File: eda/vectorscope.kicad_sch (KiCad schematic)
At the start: 76 parts, among them J1 EXT PWR, J2 IO CONNECTOR, J3 SCOPE, J4 SIGGEN, P1 IO_PLUG_USB, Q1 DMG2301L, SW1 USER, SW10 MENU, SW11 LEVEL, SW12 RANGE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

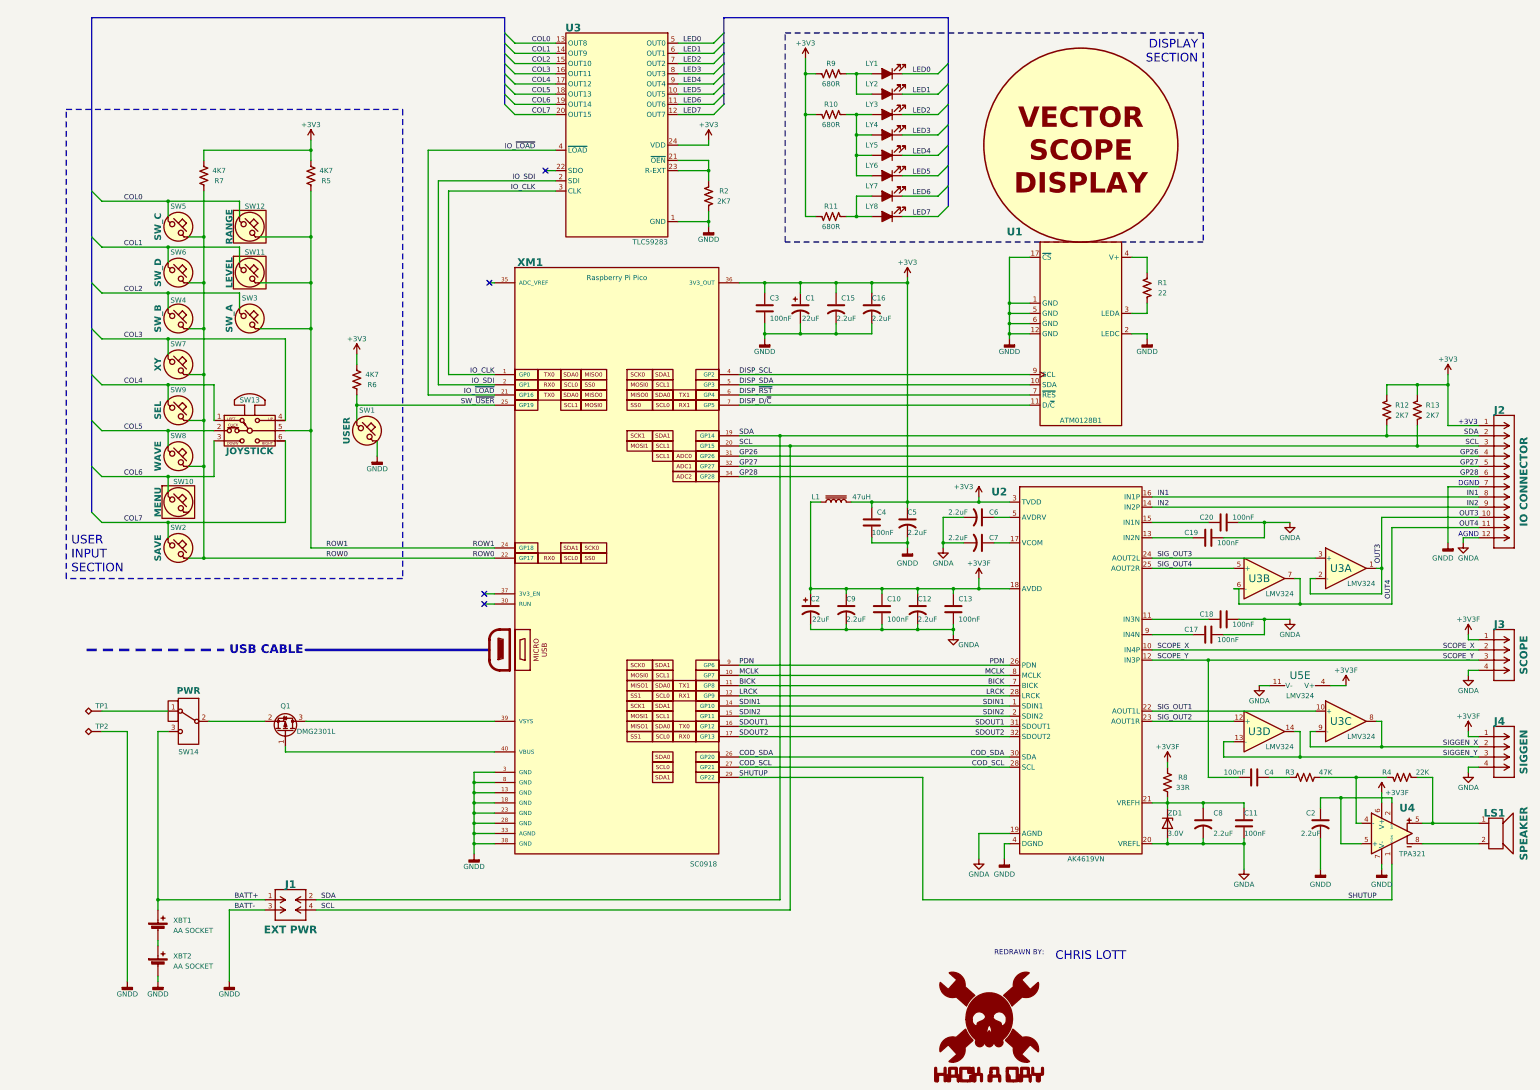
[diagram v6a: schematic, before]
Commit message: cleaned up schematic some, solved some DRC errors
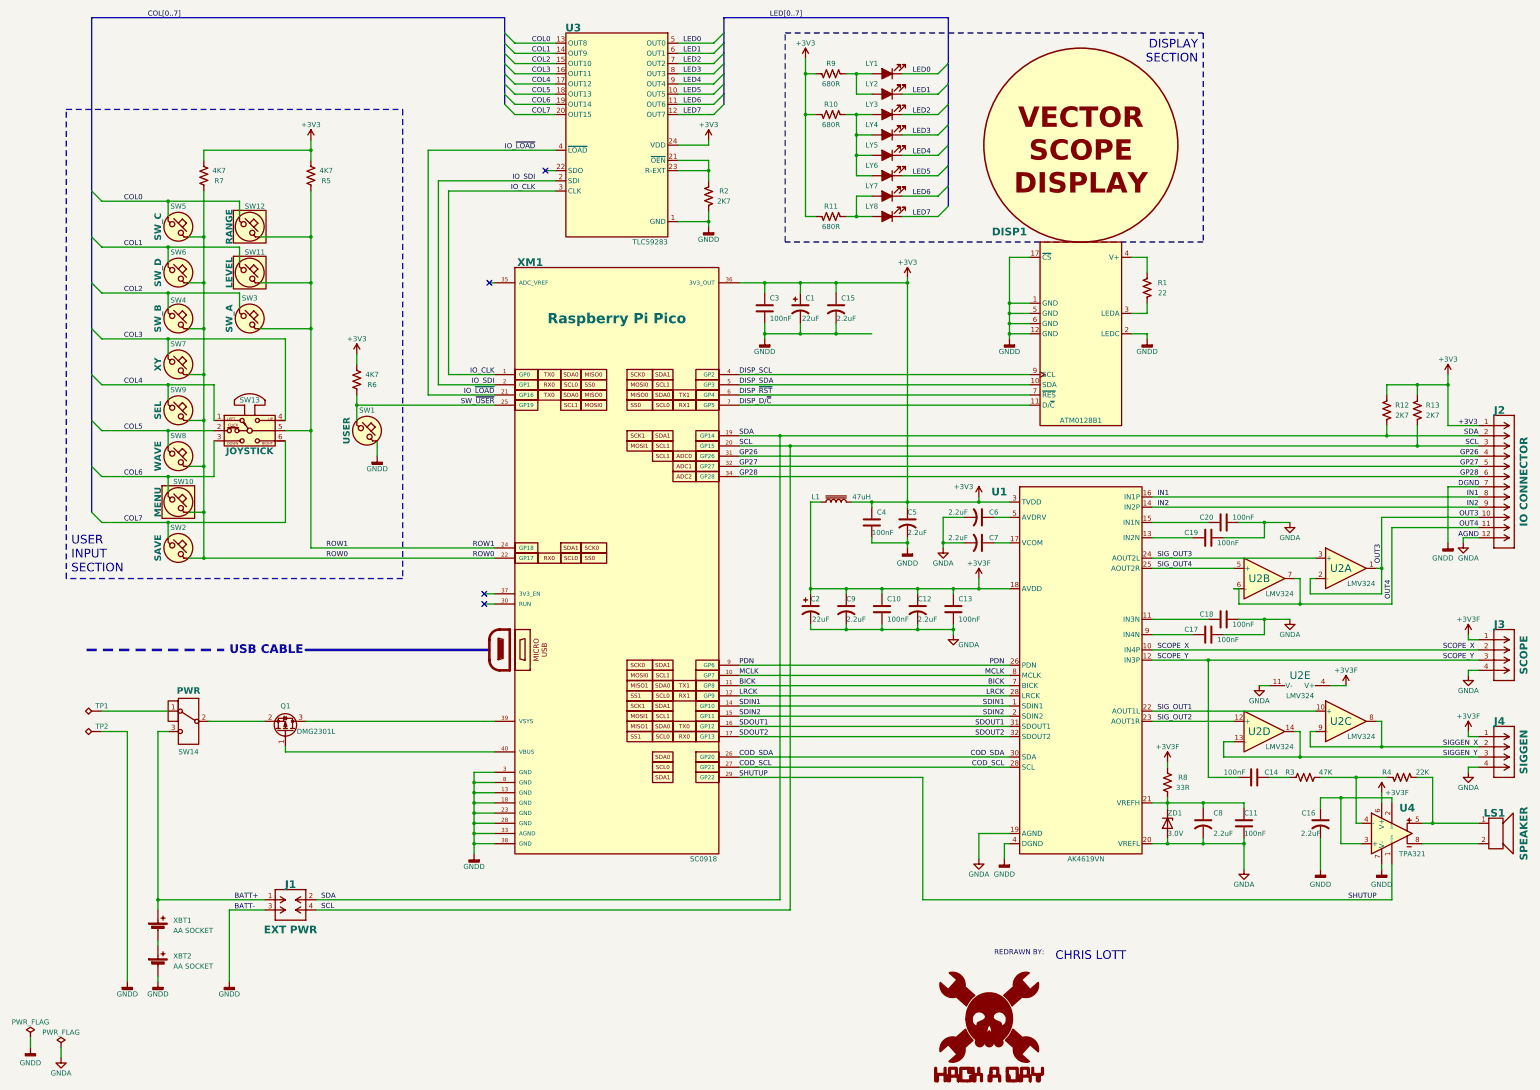
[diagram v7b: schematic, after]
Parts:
- removed C16: 2.2uF, symbol .stumbler:CAP
- P1: now left out of the parts list
- U2: renamed from U3; symbol Amplifier_Operational:LMV324 -> .vector:LMV324
- U2: renamed from U5; symbol Amplifier_Operational:LMV324 -> .vector:LMV324
- renumbered C4 to C14, C2 to C16, U1 to DISP1, U2 to U1
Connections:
- net ROW0: now also SW10.2
- net at C16.1, U4.2 (BYP): now also U4.3 (+); no longer U4.5
- net +3V3F: no longer names the net of C10.1, C12.1, C13.1, C2.1, C9.1, L1.2, U1.18 (AVDD)
- net +3V3F: no longer J3.1 (Pin_1), J4.1 (Pin_1), R8.2, U2.4 (V+), U4.6 (V+)
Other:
- note added: "BATT-"

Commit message: all schematic symbols now in local project library
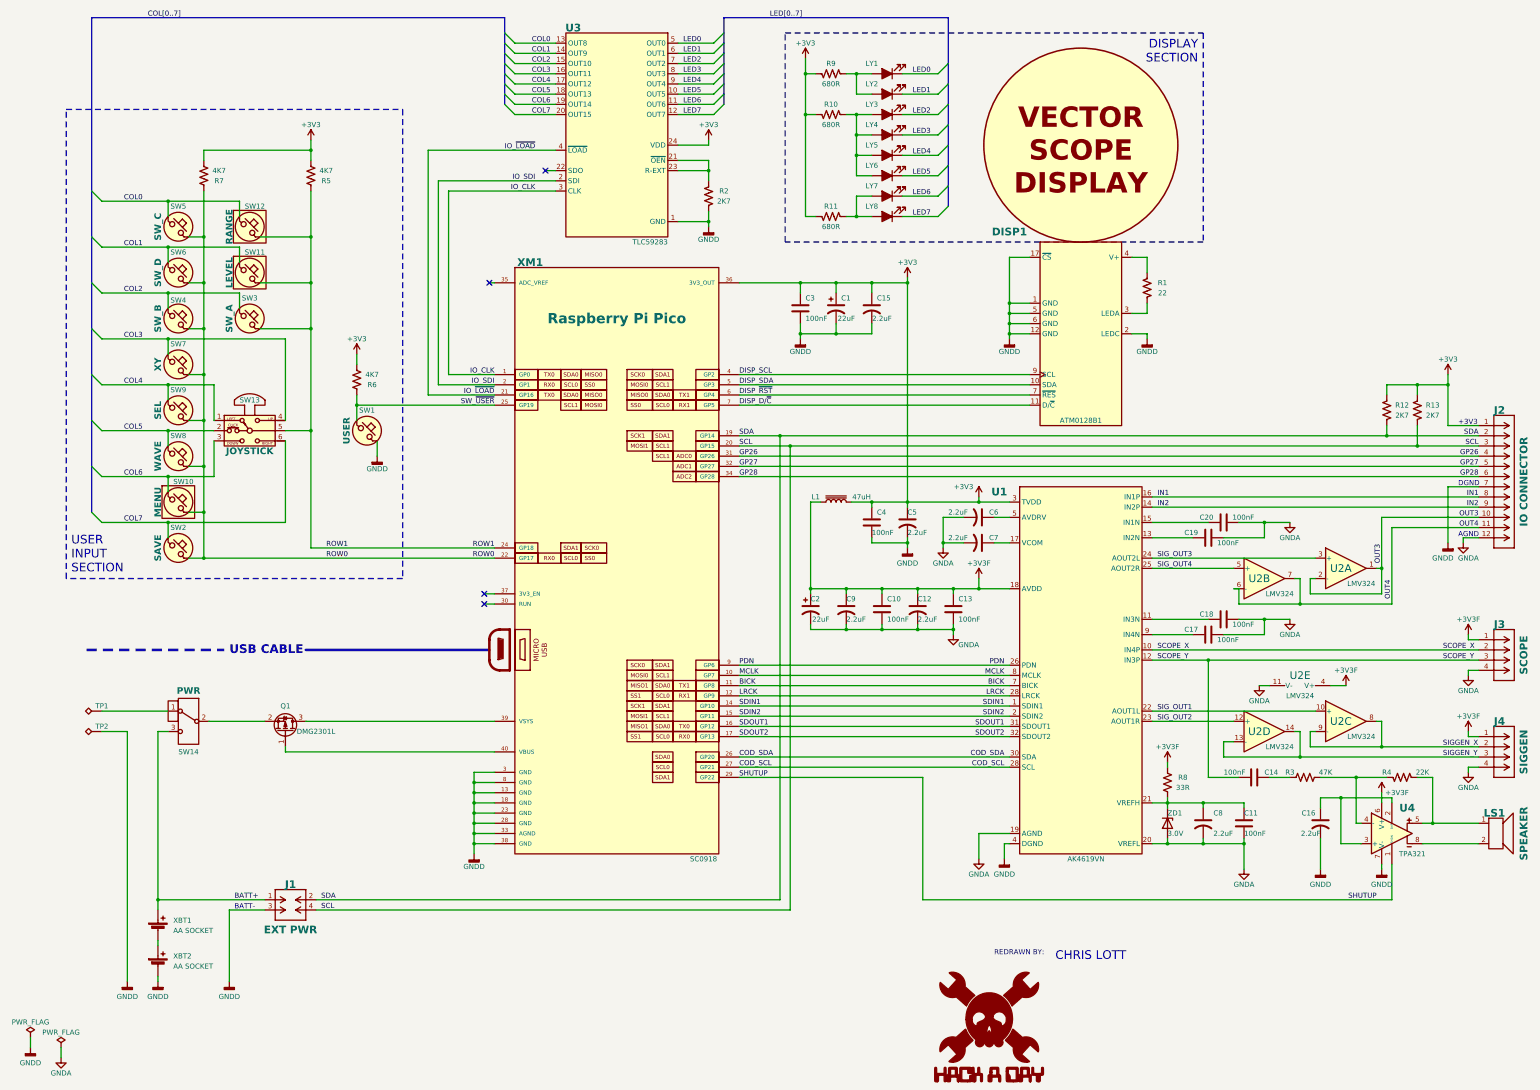
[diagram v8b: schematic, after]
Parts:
- C1, C2: symbol .stumbler:CAP_POL -> .vector:CAP_POL
- C10, C11, C13, C14, C17, C18, C19, C20, C3, C4: symbol .stumbler:C -> .vector:C
- C12, C15, C16, C5, C6, C7, C8, C9: symbol .stumbler:CAP -> .vector:CAP
- J1: symbol .stumbler:IO_JACK_M2x02B -> .vector:IO_JACK_M2x02B
- J2: symbol .stumbler:IO_JACK_M12 -> .vector:IO_JACK_M12
- J3, J4: symbol .stumbler:IO_JACK_M04 -> .vector:IO_JACK_M04
- L1: symbol .stumbler:L_Core_Iron -> .vector:L_Core_Iron
- LY1, LY2, LY3, LY4, LY5, LY6, LY7, LY8: symbol .stumbler:LED -> .vector:LED
- R1, R10, R11, R12, R13, R2, R3, R4, R5, R6, R7, R8, R9: symbol .stumbler:RES -> .vector:RES
- TP1, TP2: symbol Connector:TestPoint_Alt -> .vector:TestPoint_Alt
- XBT1, XBT2: symbol Device:Battery_Cell -> .vector:Battery_Cell
- ZD1: symbol Device:D_Zener -> .vector:D_Zener
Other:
- moved on the sheet: C1, C15, C3
